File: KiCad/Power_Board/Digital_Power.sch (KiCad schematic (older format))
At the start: 6 parts

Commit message: Updated power board schematic.
Initial schematic draft. Probably will be modified once layout is
started.
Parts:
- removed U? (x2): TPS63030, symbol TPS63030
- removed U? (x3): CS30, symbol CS30
- added C? (x9): 10uF, symbol C_Small
- added C? (x3): 0.1uF, symbol C_Small
- added L? (x3): 3.3uH, symbol INDUCTOR_SMALL
- added P? (x3): CONN_02X01, symbol CONN_02X01
- added R?: 1.8M, symbol R_Small
- added R? (x2): 200k, symbol R_Small
- added R? (x3): 0, symbol R_Small
- added R?: 1.2M, symbol R_Small
- added R?: 210k, symbol R_Small
- added R?: 520k, symbol R_Small
- added TP? (x6): Test_Point, symbol Test_Point
- added U? (x2): TPS63030, symbol TPS63030
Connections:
- net labels added: 1.8V, 3.3V, 5V, GND, Gnd, Vin
- wire segments 0 -> 92
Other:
- moved on the sheet: U?

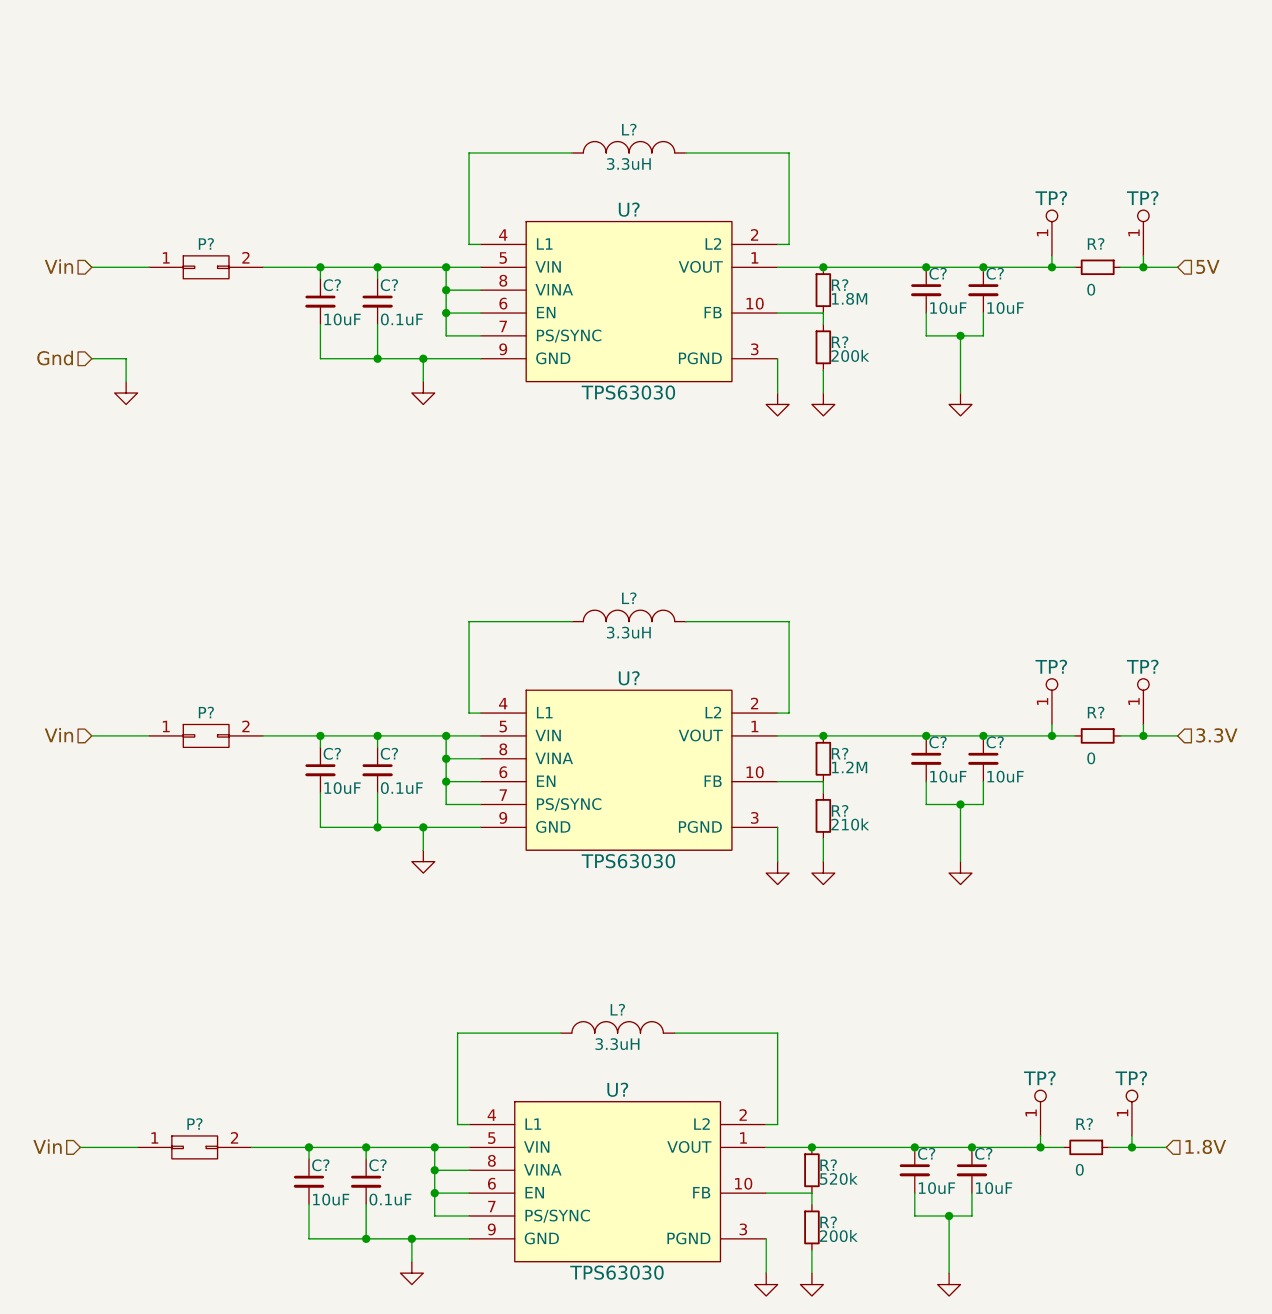
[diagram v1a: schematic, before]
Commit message: Power board fixes & Updated BOM
Initialized refdes.

Added test clip test points to all power lines (except DACs).

Fixed a feedback resistor mess up on the +/-15V LDOs.
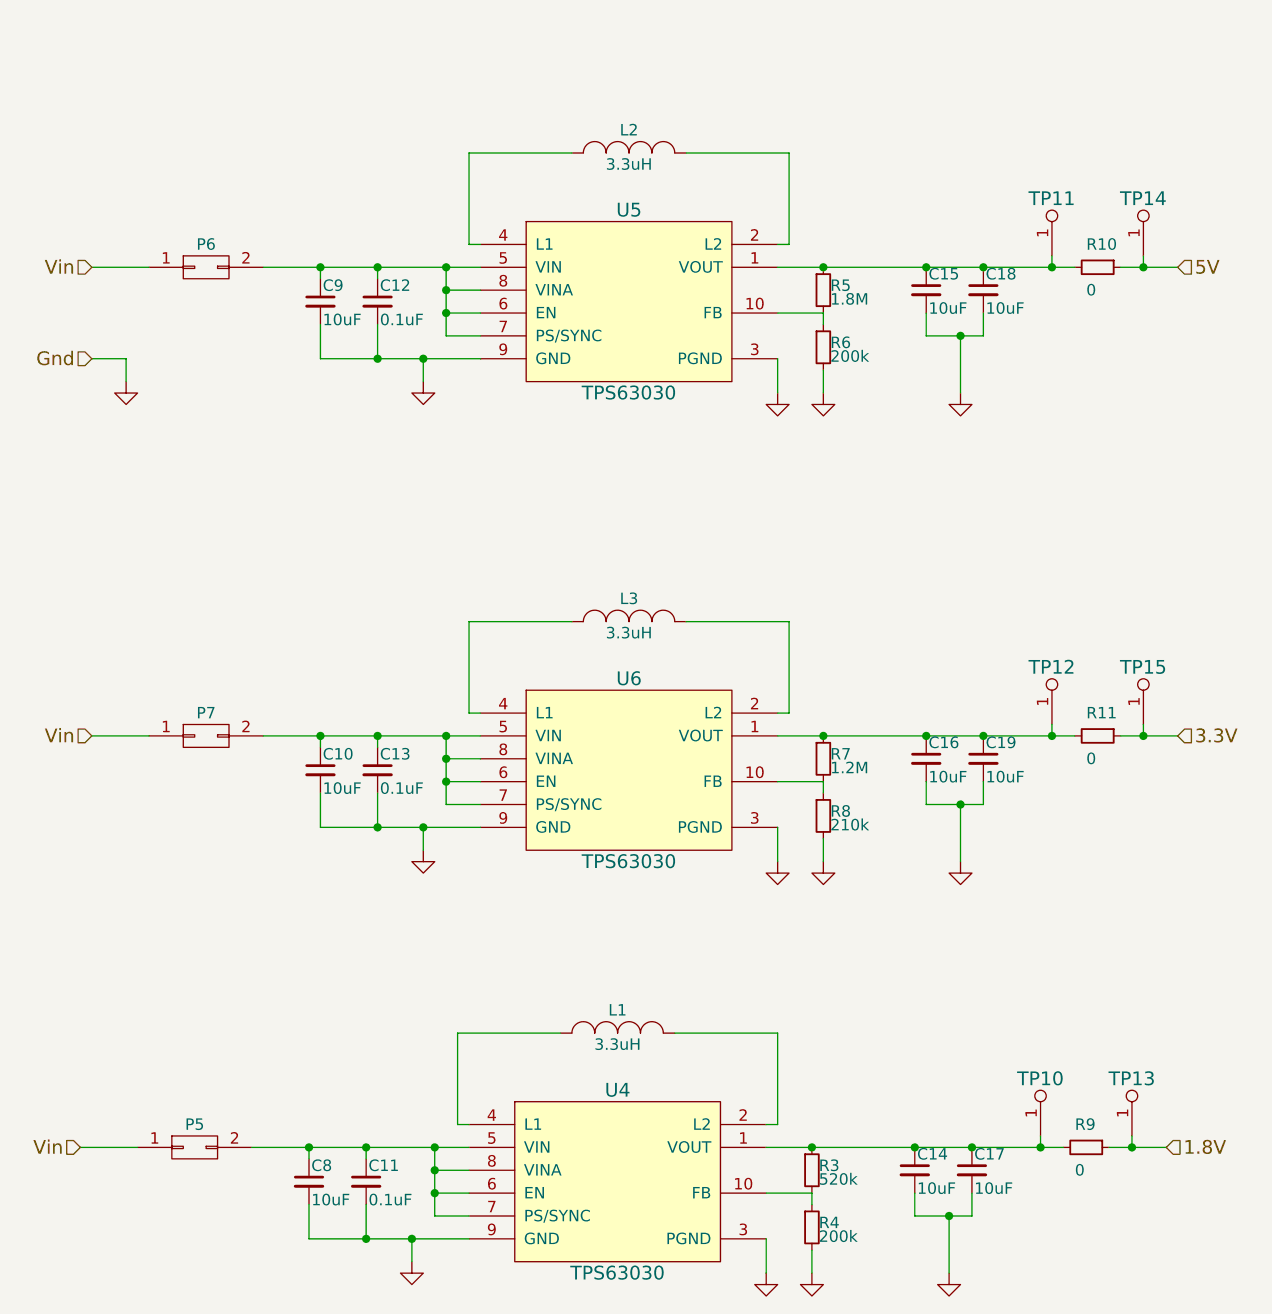
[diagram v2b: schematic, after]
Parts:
- gave numbers to parts that had none: 36

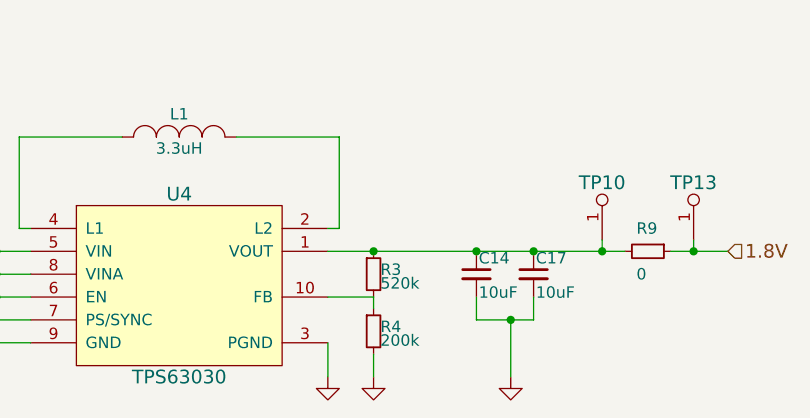
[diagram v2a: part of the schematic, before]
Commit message: Fixed -15V LDO & Updated BOM
-15V LDO had incorrect feedback resistors. +15V LDO seemed ok.

BOM updated to all tentatively selected parts.
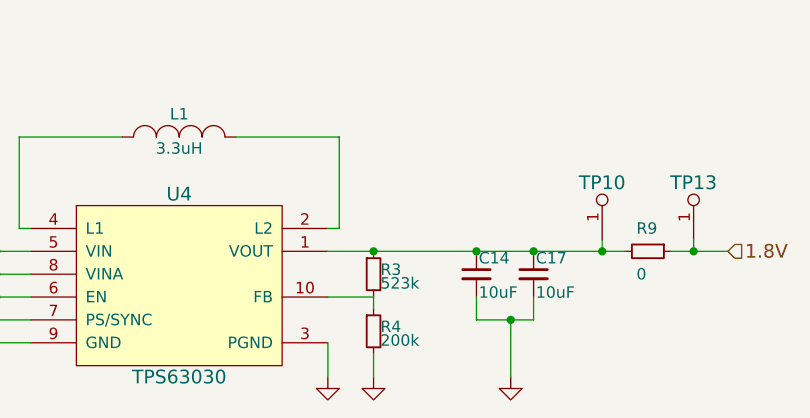
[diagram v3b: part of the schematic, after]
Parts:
- R3: value 520k -> 523k
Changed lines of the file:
@@
 P 4150 5650
 F 0 "R3" H 4180 5670 50  0000 L CNN
-F 1 "520k" H 4180 5610 50  0000 L CNN
+F 1 "523k" H 4180 5610 50  0000 L CNN
 F 2 "" H 4150 5650 60  0000 C CNN
 F 3 "" H 4150 5650 60  0000 C CNN

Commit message: Linked footprints to schematic.
Also cleaned up some footprint errors:
Changed IC footprint names to be invisible on the silkscreen layer.
Fixed test points that were lacking pin numbers causing netlist
failures.
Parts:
- C10, C14, C15, C16, C17, C18, C19, C8, C9: footprint (none) -> Capacitors_SMD:C_1210
- C11, C12, C13: footprint (none) -> Capacitors_SMD:C_0603
- L1, L2, L3: footprint (none) -> OpenCamera:NRS5030
- P5, P6, P7: footprint (none) -> OpenCamera:SMD_JUMPER
- R10, R11, R3, R4, R5, R6, R7, R8, R9: footprint (none) -> Resistors_SMD:R_0402
- TP10, TP11, TP12, TP13, TP14, TP15: footprint (none) -> OpenCamera:TEST_POINT_SMD
- U4, U5, U6: footprint (none) -> OpenCamera:TPS63030

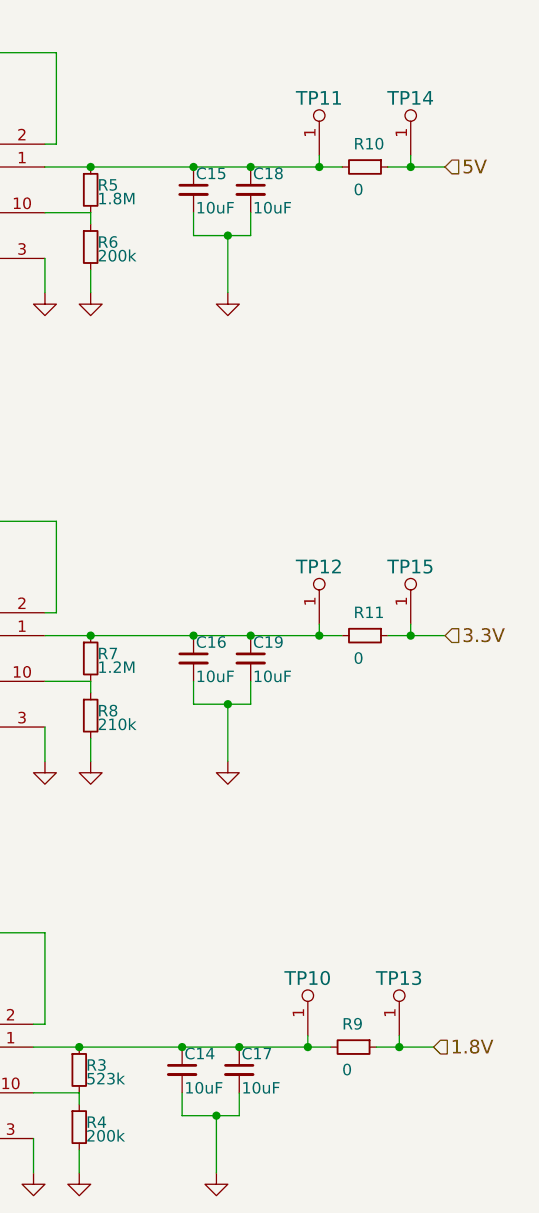
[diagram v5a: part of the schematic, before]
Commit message: Removed redundant SMD test points where test clips are being used.
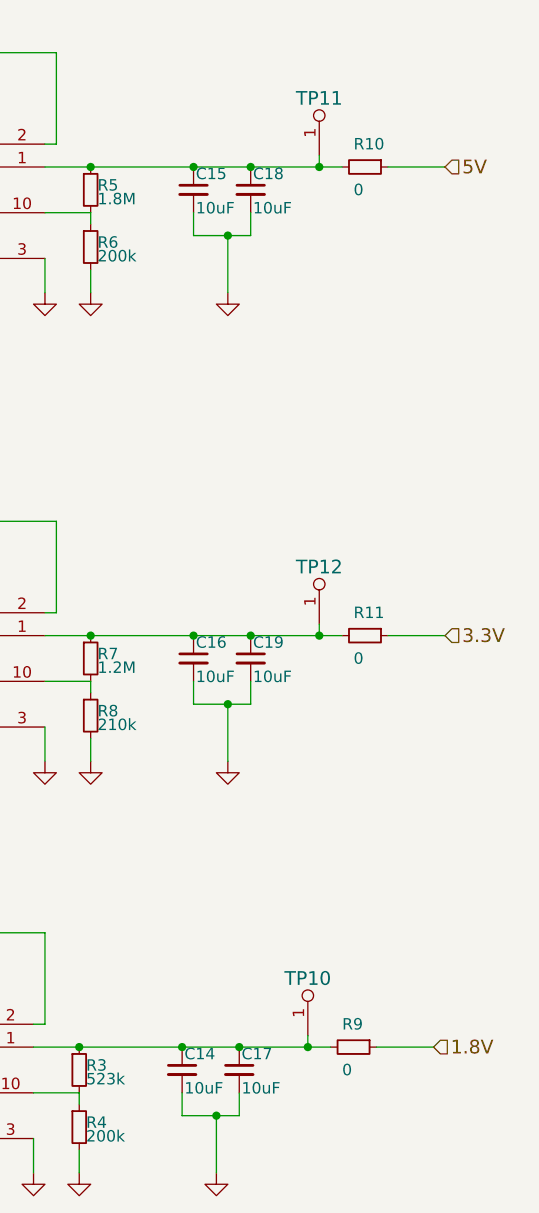
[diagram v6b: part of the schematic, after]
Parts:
- removed TP13, TP14, TP15: Test_Point, OpenCamera:TEST_POINT_SMD, symbol Test_Point
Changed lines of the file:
@@
 Connection ~ 2250 2100
 $Comp
-L GND #PWR020
+L GND #PWR022
 U 1 1 558F46DE
 P 2450 2200
-F 0 "#PWR020" H 2450 1950 50  0001 C CNN
+F 0 "#PWR022" H 2450 1950 50  0001 C CNN
 F 1 "GND" H 2450 2050 50  0001 C CNN
 F 2 "" H 2450 2200 60  0000 C CNN
@@
 	4000 1900 4200 1900
 $Comp
-L GND #PWR021
+L GND #PWR023
 U 1 1 558F4B2D
 P 4000 2250
-F 0 "#PWR021" H 4000 2000 50  0001 C CNN
+F 0 "#PWR023" H 4000 2000 50  0001 C CNN
 F 1 "GND" H 4000 2100 50  0001 C CNN
 F 2 "" H 4000 2250 60  0000 C CNN
@@
 $EndComp
 $Comp
-L GND #PWR022
+L GND #PWR024
 U 1 1 558F4B9B
 P 4200 2250
-F 0 "#PWR022" H 4200 2000 50  0001 C CNN
+F 0 "#PWR024" H 4200 2000 50  0001 C CNN
 F 1 "GND" H 4200 2100 50  0001 C CNN
 F 2 "" H 4200 2250 60  0000 C CNN
@@
 $EndComp
 $Comp
-L GND #PWR023
+L GND #PWR025
 U 1 1 558F4BB8
 P 4800 2250
-F 0 "#PWR023" H 4800 2000 50  0001 C CNN
+F 0 "#PWR025" H 4800 2000 50  0001 C CNN
 F 1 "GND" H 4800 2100 50  0001 C CNN
 F 2 "" H 4800 2250 60  0000 C CNN
@@
 	1    0    0    -1
 $EndComp
-$Comp
-L Test_Point TP14
-U 1 1 558F6F2F
-P 5600 1650
-F 0 "TP14" H 5600 1900 60  0000 C CNN
-F 1 "Test_Point" H 5600 2000 60  0001 C CNN
-F 2 "OpenCamera:TEST_POINT_SMD" H 5600 1650 60  0001 C CNN
-F 3 "" H 5600 1650 60  0000 C CNN
-	1    5600 1650
-	1    0    0    -1
-$EndComp
 Wire Wire Line
 	5200 1650 5200 1700
 Connection ~ 5200 1700
-Wire Wire Line
-	5600 1650 5600 1700
-Connection ~ 5600 1700
 $Comp
 L TPS63030 U6
@@
 Connection ~ 2250 4150
 $Comp
-L GND #PWR024
+L GND #PWR026
 U 1 1 558F7738
 P 2450 4250
-F 0 "#PWR024" H 2450 4000 50  0001 C CNN
+F 0 "#PWR026" H 2450 4000 50  0001 C CNN
 F 1 "GND" H 2450 4100 50  0001 C CNN
 F 2 "" H 2450 4250 60  0000 C CNN
@@
 	4000 3950 4200 3950
 $Comp
-L GND #PWR025
+L GND #PWR027
 U 1 1 558F774F
 P 4000 4300
-F 0 "#PWR025" H 4000 4050 50  0001 C CNN
+F 0 "#PWR027" H 4000 4050 50  0001 C CNN
 F 1 "GND" H 4000 4150 50  0001 C CNN
 F 2 "" H 4000 4300 60  0000 C CNN
@@
 $EndComp
 $Comp
-L GND #PWR026
+L GND #PWR028
 U 1 1 558F7755
 P 4200 4300
-F 0 "#PWR026" H 4200 4050 50  0001 C CNN
+F 0 "#PWR028" H 4200 4050 50  0001 C CNN
 F 1 "GND" H 4200 4150 50  0001 C CNN
 F 2 "" H 4200 4300 60  0000 C CNN
@@
 $EndComp
 $Comp
-L GND #PWR027
+L GND #PWR029
 U 1 1 558F775B
 P 4800 4300
-F 0 "#PWR027" H 4800 4050 50  0001 C CNN
+F 0 "#PWR029" H 4800 4050 50  0001 C CNN
 F 1 "GND" H 4800 4150 50  0001 C CNN
 F 2 "" H 4800 4300 60  0000 C CNN
@@
 	1    0    0    -1
 $EndComp
-$Comp
-L Test_Point TP15
-U 1 1 558F777A
-P 5600 3700
-F 0 "TP15" H 5600 3950 60  0000 C CNN
-F 1 "Test_Point" H 5600 4050 60  0001 C CNN
-F 2 "OpenCamera:TEST_POINT_SMD" H 5600 3700 60  0001 C CNN
-F 3 "" H 5600 3700 60  0000 C CNN
-	1    5600 3700
-	1    0    0    -1
-$EndComp
 Wire Wire Line
 	5200 3700 5200 3750
 Connection ~ 5200 3750
-Wire Wire Line
-	5600 3700 5600 3750
-Connection ~ 5600 3750
 $Comp
 L TPS63030 U4
@@
 Connection ~ 2200 5950
 $Comp
-L GND #PWR028
+L GND #PWR030
 U 1 1 558F7A10
 P 2400 6050
-F 0 "#PWR028" H 2400 5800 50  0001 C CNN
+F 0 "#PWR030" H 2400 5800 50  0001 C CNN
 F 1 "GND" H 2400 5900 50  0001 C CNN
 F 2 "" H 2400 6050 60  0000 C CNN
@@
 	3950 5750 4150 5750
 $Comp
-L GND #PWR029
+L GND #PWR031
 U 1 1 558F7A27
 P 3950 6100
-F 0 "#PWR029" H 3950 5850 50  0001 C CNN
+F 0 "#PWR031" H 3950 5850 50  0001 C CNN
 F 1 "GND" H 3950 5950 50  0001 C CNN
 F 2 "" H 3950 6100 60  0000 C CNN
@@
 $EndComp
 $Comp
-L GND #PWR030
+L GND #PWR032
 U 1 1 558F7A2D
 P 4150 6100
-F 0 "#PWR030" H 4150 5850 50  0001 C CNN
+F 0 "#PWR032" H 4150 5850 50  0001 C CNN
 F 1 "GND" H 4150 5950 50  0001 C CNN
 F 2 "" H 4150 6100 60  0000 C CNN
@@
 $EndComp
 $Comp
-L GND #PWR031
+L GND #PWR033
 U 1 1 558F7A33
 P 4750 6100
-F 0 "#PWR031" H 4750 5850 50  0001 C CNN
+F 0 "#PWR033" H 4750 5850 50  0001 C CNN
 F 1 "GND" H 4750 5950 50  0001 C CNN
 F 2 "" H 4750 6100 60  0000 C CNN
@@
 	1    0    0    -1
 $EndComp
-$Comp
-L Test_Point TP13
-U 1 1 558F7A52
-P 5550 5500
-F 0 "TP13" H 5550 5750 60  0000 C CNN
-F 1 "Test_Point" H 5550 5850 60  0001 C CNN
-F 2 "OpenCamera:TEST_POINT_SMD" H 5550 5500 60  0001 C CNN
-F 3 "" H 5550 5500 60  0000 C CNN
-	1    5550 5500
-	1    0    0    -1
-$EndComp
 Wire Wire Line
 	5150 5500 5150 5550
 Connection ~ 5150 5550
-Wire Wire Line
-	5550 5500 5550 5550
-Connection ~ 5550 5550
-$Comp
-L GND #PWR032
+$Comp
+L GND #PWR034
 U 1 1 558F8FF0
 P 1150 2200
-F 0 "#PWR032" H 1150 1950 50  0001 C CNN
+F 0 "#PWR034" H 1150 1950 50  0001 C CNN
 F 1 "GND" H 1150 2050 50  0001 C CNN
 F 2 "" H 1150 2200 60  0000 C CNN

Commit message: Component changes
Switched Vref test point to test clip.
Beefed up 0ohm jumpers to 0805.
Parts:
- R10, R11, R9: footprint Resistors_SMD:R_0402 -> Resistors_SMD:R_0805
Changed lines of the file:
@@
 F 0 "R10" V 5300 1650 50  0000 L CNN
 F 1 "0" V 5500 1650 50  0000 L CNN
-F 2 "Resistors_SMD:R_0402" H 5400 1700 60  0001 C CNN
+F 2 "Resistors_SMD:R_0805" H 5400 1700 60  0001 C CNN
 F 3 "" H 5400 1700 60  0000 C CNN
 	1    5400 1700
@@
 F 0 "R11" V 5300 3700 50  0000 L CNN
 F 1 "0" V 5500 3700 50  0000 L CNN
-F 2 "Resistors_SMD:R_0402" H 5400 3750 60  0001 C CNN
+F 2 "Resistors_SMD:R_0805" H 5400 3750 60  0001 C CNN
 F 3 "" H 5400 3750 60  0000 C CNN
 	1    5400 3750
@@
 F 0 "R9" V 5250 5500 50  0000 L CNN
 F 1 "0" V 5450 5500 50  0000 L CNN
-F 2 "Resistors_SMD:R_0402" H 5350 5550 60  0001 C CNN
+F 2 "Resistors_SMD:R_0805" H 5350 5550 60  0001 C CNN
 F 3 "" H 5350 5550 60  0000 C CNN
 	1    5350 5550
